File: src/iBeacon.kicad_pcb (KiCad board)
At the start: 2 copper layers, 30 x 26.1 mm, 8 parts, among them IC1 AE-TYBLE16, P1 CONN_01X02, P2 CONN_01X02, P3 CONN_01X02

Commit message: 2nd Version
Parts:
- added IC2: ATTINY10-TSHR, ATTINY10-TSHR:SOT95P280X145-6N, F.Cu at (172.4, 110.8)
- added JP1: JUMPER, solderjumper:SolderJumper-2_P1.3mm_Open_Pad1.0x1.5mm, F.Cu at (169.2, 114.2)
- added P4: CONN_01X03, Pin_Headers:Pin_Header_Angled_1x03_Pitch2.54mm, F.Cu at (173.2, 101.4)
- D1: footprint LEDs:LED_1206_HandSoldering -> LEDs:LED_0603_HandSoldering
- R1: footprint Resistors_SMD:R_1206_HandSoldering -> Resistors_SMD:R_0603_HandSoldering
- moved D1 16.1 mm to (166.1, 93.7), turned to 180 degrees
- moved R1 13.7 mm to (161.7, 93.7), turned to 180 degrees
- moved P2 0.41 mm to (168.6, 111.1)
- moved P3 0.38 mm to (168.6, 101.4)
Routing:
- net Net-(Battery1-Pad2): track 110.7 -> 66.8 mm, vias 14 -> 12
- net Net-(Battery1-Pad1): track 9.88 -> 29.7 mm, vias 0 -> 2
- net Net-(IC1-Pad15): track 20.8 -> 7.88 mm
- net Net-(IC2-Pad3): track 0.00 -> 8.90 mm
- net Net-(IC2-Pad1): track 0.00 -> 6.72 mm
- net Net-(IC2-Pad6): track 0.00 -> 5.72 mm, vias 0 -> 1
- net Net-(IC2-Pad4): track 0.00 -> 3.36 mm
- net Net-(IC1-Pad2): track 3.76 -> 6.42 mm
- net Net-(D1-Pad2): track 2.88 -> 2.25 mm
- net Net-(IC1-Pad6): track 4.74 -> 4.19 mm
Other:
- net class Default: trace_width 0.5 -> 0.6
- net class Wide: trace_width 0.5 -> 0.6
- board text added: "At programming, JP1 must be cuted off."
- board text added: "IC2: ATTINY10-TSHR R1: 4K(0603) D1: LED(0603)"
- board text added: "PB0"
- board text added: "PB1"
- board text added: "RST"
- board text removed: "1206"

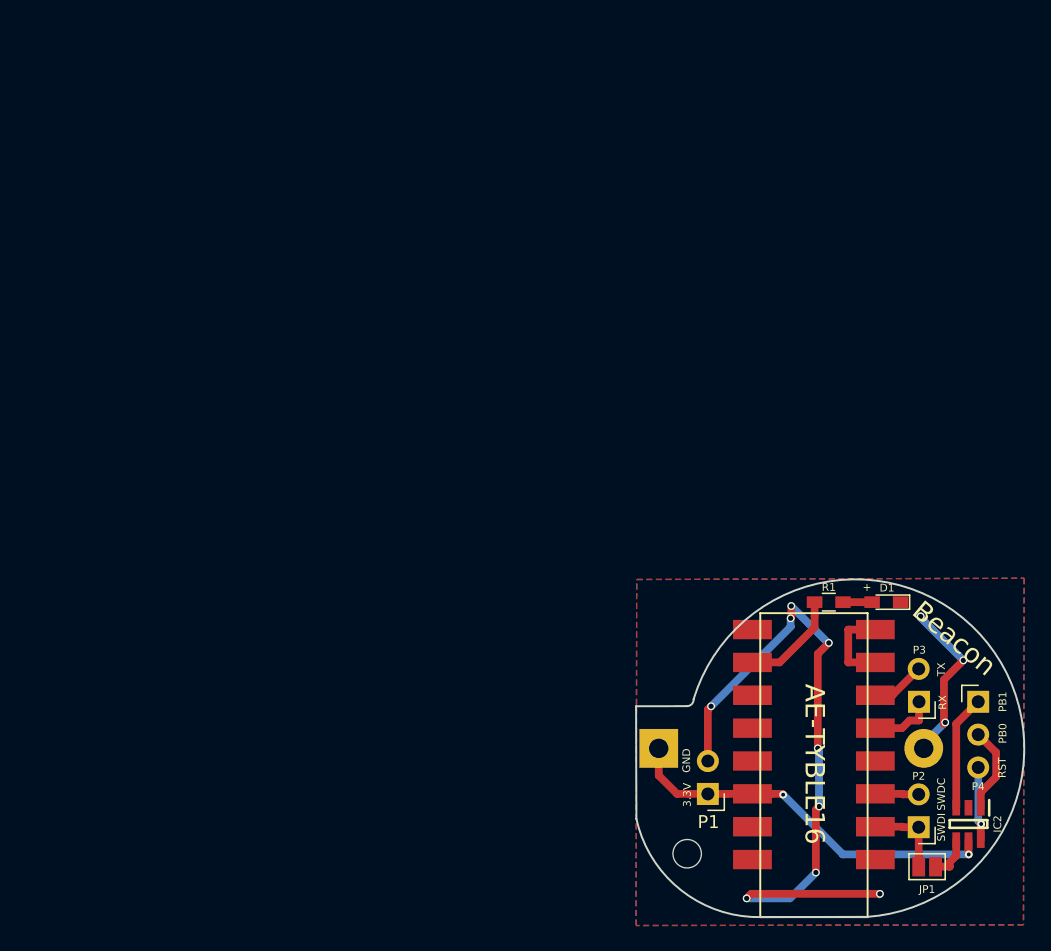
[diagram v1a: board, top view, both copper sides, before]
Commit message: Redesigning board
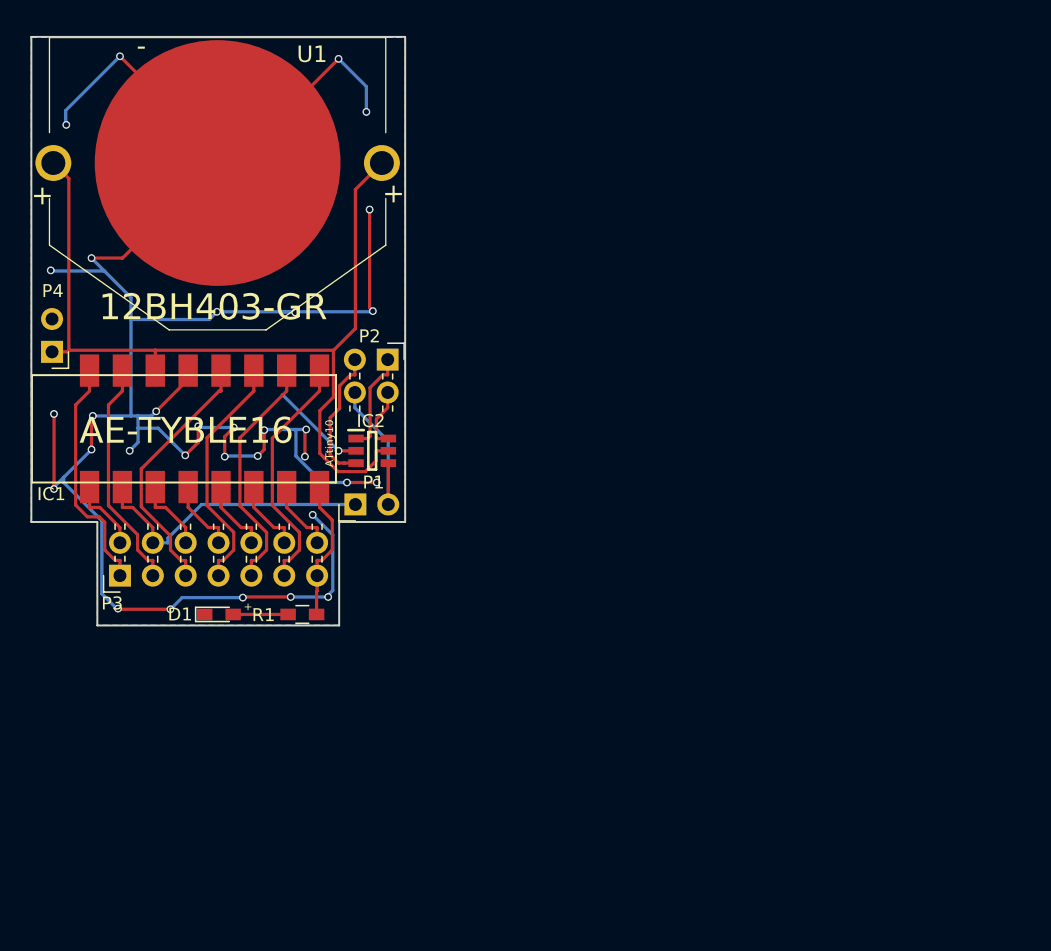
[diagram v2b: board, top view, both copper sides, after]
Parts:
- removed Battery1: CONN_01X02, Battery_Holders:Keystone_104_1x23mm-CoinCell
- removed JP1: JUMPER, solderjumper:SolderJumper-2_P1.3mm_Open_Pad1.0x1.5mm
- removed REF01: MountingHole_2.2mm_M2_DIN965, Mounting_Holes:MountingHole_2.2mm_M2_DIN965
- added U1: 12BH403-GR, 12BH403GR, F.Cu at (114.4, 61.4)
- P2: value CONN_01X02 -> CONN_02X02; footprint Pin_Headers:Pin_Header_Angled_1x02_Pitch2.54mm -> Pin_Headers:Pin_Header_Angled_2x02_Pitch2.54mm
- P3: value CONN_01X02 -> CONN_02X07; footprint Pin_Headers:Pin_Header_Angled_1x02_Pitch2.54mm -> Pin_Headers:Pin_Header_Angled_2x07_Pitch2.54mm
- P4: value CONN_01X03 -> CONN_01X02; footprint Pin_Headers:Pin_Header_Angled_1x03_Pitch2.54mm -> Pin_Headers:Pin_Header_Angled_1x02_Pitch2.54mm
- moved P4 76.5 mm to (101.6, 74.3), turned to 180 degrees
- moved P3 62.5 mm to (106.8, 91.7), turned to 90 degrees
- moved IC1 55.2 mm to (111.8, 80.3), turned to 90 degrees
- moved P2 54.7 mm to (127.5, 75.0), turned to 270 degrees
- moved IC2 54.4 mm to (126.3, 82.0), turned to 0 degrees
- moved D1 51.6 mm to (114.5, 94.7), turned to 0 degrees
- moved R1 40.7 mm to (121.0, 94.7), turned to 0 degrees
- moved P1 35.3 mm to (125.0, 86.2), turned to 90 degrees
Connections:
- D1 pad 1: Net-(Battery1-Pad2) -> Net-(D1-Pad1)
- IC1 pad 1: (no net) -> Net-(IC1-Pad1)
- IC1 pad 10: (no net) -> Net-(IC1-Pad10)
- IC1 pad 11: Net-(Battery1-Pad1) -> Net-(IC1-Pad11)
- IC1 pad 12: Net-(Battery1-Pad2) -> Net-(D1-Pad1)
- IC1 pad 13: (no net) -> Net-(IC1-Pad13)
- IC1 pad 14: (no net) -> Net-(IC1-Pad14)
- IC1 pad 16: (no net) -> Net-(IC1-Pad16)
- IC1 pad 4: (no net) -> Net-(IC1-Pad4)
- IC1 pad 8: Net-(IC1-Pad7) -> Net-(IC1-Pad8)
- IC1 pad 9: (no net) -> Net-(IC1-Pad9)
- IC2 pad 2: Net-(Battery1-Pad2) -> Net-(D1-Pad1)
- IC2 pad 5: Net-(Battery1-Pad1) -> Net-(IC1-Pad11)
- P1 pad 1: Net-(Battery1-Pad1) -> Net-(IC1-Pad2)
- P1 pad 2: Net-(Battery1-Pad2) -> Net-(IC2-Pad4)
- P2 pad 1: Net-(IC1-Pad2) -> Net-(IC2-Pad1)
- P2 pad 2: Net-(IC1-Pad3) -> Net-(IC2-Pad6)
- P3 pad 1: Net-(IC1-Pad5) -> Net-(IC1-Pad9)
- P3 pad 2: Net-(IC1-Pad6) -> Net-(IC1-Pad1)
- P4 pad 1: Net-(IC2-Pad3) -> Net-(IC1-Pad11)
- P4 pad 2: Net-(IC2-Pad1) -> Net-(D1-Pad1)
- R1 pad 2: Net-(IC1-Pad15) -> Net-(IC1-Pad8)
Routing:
- net Net-(D1-Pad1): track 0.00 -> 195.4 mm, vias 0 -> 33
- net Net-(IC1-Pad11): track 0.00 -> 69.8 mm
- net Net-(Battery1-Pad2): track 66.8 -> 0.00 mm, vias 12 -> 0
- net Net-(Battery1-Pad1): track 29.7 -> 0.00 mm, vias 2 -> 0
- net Net-(IC1-Pad13): track 0.00 -> 20.1 mm
- net Net-(IC1-Pad16): track 0.00 -> 18.9 mm
- net Net-(IC1-Pad14): track 0.00 -> 18.9 mm
- net Net-(IC1-Pad9): track 0.00 -> 18.5 mm
- net Net-(IC1-Pad10): track 0.00 -> 17.9 mm
- net Net-(IC1-Pad2): track 6.42 -> 22.8 mm
- net Net-(IC1-Pad15): track 7.88 -> 18.9 mm
- net Net-(IC1-Pad8): track 0.00 -> 11.0 mm
- net Net-(IC2-Pad4): track 3.36 -> 12.9 mm
- net Net-(IC1-Pad4): track 0.00 -> 5.75 mm
- net Net-(IC1-Pad1): track 0.00 -> 5.75 mm
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- added copper zone on B.Cu, net Net-(D1-Pad1)
- added copper zone on F.Cu, net Net-(D1-Pad1)
- removed copper zone on B.Cu, net Net-(Battery1-Pad2)
- removed copper zone on F.Cu, net Net-(Battery1-Pad2)
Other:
- board size 30 x 26.1 mm -> 28.9 x 45.5 mm
- net class Default: trace_width 0.6 -> 0.25
- net class Wide: trace_width 0.6 -> 0.25
- board text added: "-"
- board text added: "12BH403-GR"
- board text added: "ATtiny10"
- board text added: "Beacon V0.3"
- board text added: "Case: Takachi PS-64 R1/D1: 0603"
- board text added: "In programming, P1 must be cutted off."
- board text added: "P000"
- board text added: "P001"
- board text added: "P002"
- board text added: "P003"
- board text added: "P004"
- board text added: "P005"
- board text added: "P006"
- board text added: "P017"
- board text added: "P019"
- board text added: "P021"
- board text added: "P023"
- board text added: "P025"
- board text added: "PB2"
- board text added: "PB3"
- board text added: "https://github.com/MypaceEngine/ ae-tyble16-beacon"
- board text removed: "At programming, JP1 must be cuted off."
- board text removed: "Beacon"
- board text removed: "Deploy Button Battery Holder on this side"
- board text removed: "IC2: ATTINY10-TSHR R1: 4K(0603) D1: LED(0603)"
- board text removed: "RST"
- board text removed: "RX"
- board text removed: "TX"
- board text removed: "https://github.com/MypaceEngine/ ae-tyble16-beacon.git"
